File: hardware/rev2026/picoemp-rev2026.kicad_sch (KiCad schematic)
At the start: 53 parts, among them J1 EDGE-SMA, J2 1x2_Pin_Header, J3 MKDS 1,5/2-5.08, J4 EDGE-SMA, P1 Header 7, P2 Header 2, P3 Header 4, Q1 LDA111STR, Q2 RGT16BM65DTL, Q3 AO3422, Q4 AO3422, SW1 KSC741J LFS, SW2 KSC741J LFS, SW3 TL3301AF160QJ, T1 ATB322524, T2 ATB322524, U1 SC0915, U2 74LVC1G17

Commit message: Netclass widths, verified DRC rules, and outline repair
Board setup for routing:

* HV netclass gets real copper -- 0.5 mm default track, 0.8/0.4 via. Its
  clearance stays 0.2 mm; the 1 mm isolation barrier remains a scoped custom
  rule, not a netclass value.
* New Power class (GND, +3V3) at 0.4 mm / 0.8-0.4 via.
* Predefined track widths 0.2/0.3/0.4/0.5/0.8/1.0 and via sizes so W and V
  cycle useful values while routing.

Deliberately NOT splitting an HV_PULSE class out of HV. KiCad 10 resolves each
net to exactly one effective netclass -- an experiment with an overlapping
HV_PULSE showed hasNetclass('HV_PULSE') never matching while hasNetclass('HV')
still did. Splitting the discharge-loop nets out would risk dropping the two
highest-energy nets on the board out of the isolation-barrier rule, to buy
nothing but a router default width. Route those wide by hand or with a pour.

Custom rules, each confirmed to actually fire against this board:

* Barrier and edge rules now use hasNetclass('HV') so they cannot develop a
  hole if a net ever picks up an additional class.
* Advisory (warning-severity) 0.4 mm minimum on HV track width. Advisory
  because KiCad has no auto-neck and necking into a pad is legitimate.
* Documented exceptions for geometry the layout does not control: edge-mount
  SMA pads on J1/J4, ATB3225 intra-package spacing on T1/T2, TO-252 tab-to-lead
  spacing on Q2.

Two DRU behaviours worth recording, both verified rather than assumed:

* The LAST matching rule wins, so exceptions must sit below the broad rules.
  Placed above, they are silently overridden.
* An unknown function in a condition is NOT an error. memberOf() -- the pre-v7
  spelling of memberOfFootprint() -- parses, reports nothing and never matches,
  so a rule can look present while enforcing nothing.

Also repaired the two remaining 0.020 mm Edge.Cuts gaps at the top corners. The
earlier outline fix removed four degenerate stub segments but only re-joined the
two at the bottom, so in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
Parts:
- MH1, MH2, MH3: footprint MountingHole:MountingHole_3.2mm_M3 -> MountingHole:MountingHole_3.2mm_M3_Pad_Via
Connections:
- no-connect marks 27 -> 24

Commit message: Name every net; scope the HV class by an HV_* wildcard
Replaced all 20 auto-generated net names with meaningful ones by adding local
labels to the schematic, and propagated them to the board.

    HV_RAIL       <- Net-(D2-K)        +250 V rail: C3+, D2 K, J1 shell, R2
    HV_RTN        <- Net-(D7-A)        isolated HV return
    HV_RECT       <- Net-(D2-A)        T1 secondary -> D2 anode
    HV_OUT        <- Net-(J1-Ext)      Q2 collector -> SMA centre (the pulse)
    HV_SENSE      <- Net-(J3-Pin_2)    divider tap, J3 pin 2
    HV_SENSE_LED  <- Net-(Q1-A)        R1 -> Q1 opto LED anode
    HV_GATE       <- Net-(D7-K)        Q2 gate, clamped by D7
    HV_GATE_DRV   <- Net-(R7-Pad2)     T2 secondary -> gate series R7
    T1_PRI_A/B, T2_PRI_A/B, PRI_CLAMP, Q3_GATE, Q4_GATE,
    VEXT_IN, VBUS, LED_HV_DET_A, LED_STATUS_A, LED_CHARGE_A

The HV_ prefix is load-bearing, not cosmetic. Every net in the isolated HV
domain now carries it, so a single "HV_*" netclass pattern covers all of them
and a newly added HV net cannot be silently left out of the 1 mm barrier.

That had already happened. The opto LED anode -- then Net-(Q1-A) -- sits
entirely on the HV side of Q1, between R1 and the LED, and was NOT in the HV
class. DRC would have permitted logic copper 0.2 mm from a node that floats
with the HV return. The netlist shows the domain is galvanically isolated: T1,
T2 and Q1 are the only crossings, and GND appears on no HV net.

Verified rather than assumed:
* Net membership is byte-identical for all 20 renamed nets, and the whole
  schematic net partition is unchanged, so connectivity did not move.
* The HV_* wildcard really resolves -- board pads now report netclass 'HV' for
  the renamed nets. A pattern that silently matched nothing would have left the
  barrier inert with no error.
* The symbol->schematic pin transform was not guessed. Scoring pins against
  wire endpoints could not decide it (a symmetric 2-pin part lands on a valid
  endpoint under either convention), so i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
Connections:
- net LED_STATUS_A: now reaches D8.2 (A), R12.2
- net LED_CHARGE_A: now reaches D9.2 (A), R13.2
- net T2_PRI_B: now reaches C5.2, R3.1, T2.4
- net HV_RTN: now reaches C3.1, D7.2 (A), J3.1 (Pin_1), Q1.2 (K), Q2.3 (E), R9.1, SW3.1, T1.3, T2.2
- net HV_SENSE: now reaches J3.2 (Pin_2), R1.1, R2.2, SW3.2
- net PRI_CLAMP: now reaches D3.1 (K), R3.2, R4.2
- net Q3_GATE: now reaches D4.1 (K), Q3.1 (G), R5.2
- net Q4_GATE: now reaches D5.1 (K), Q4.1 (G), R10.2
- net T1_PRI_B: now reaches C1.2, C2.2, R4.1, T1.4
- net HV_RAIL: now reaches C3.2, D2.1 (K), J1.1 (In), R2.1
- net HV_RECT: now reaches D2.2 (A), T1.2
- net HV_GATE: now reaches D7.1 (K), Q2.1 (G), R7.1
- net HV_OUT: now reaches J1.2 (Ext), Q2.2 (C)
- net T1_PRI_A: now reaches Q3.3 (D), T1.1
- net HV_GATE_DRV: now reaches R7.2, R9.2, T2.3
- net LED_HV_DET_A: now reaches D6.2 (A), R11.2
- net T2_PRI_A: now reaches Q4.3 (D), T2.1
- net HV_SENSE_LED: now reaches Q1.1 (A), R1.2
- net VEXT_IN: now reaches D1.2 (A), J2.1 (Pin_1)
- net VBUS: now reaches D1.1 (K), U1.40 (VBUS)
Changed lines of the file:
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@@
 	)
 	(embedded_fonts no)
+	(label "T1_PRI_B"
+		(at 274.32 294.64 0)
+		(effects
+			(font
+				(size 1.27 1.27)
+			)
+			(justify left bottom)
+		)
+	)
+	(label "T2_PRI_B"
+		(at 279.4 353.06 0)
+		(effects
+			(font
+				(size 1.27 1.27)
+			)
+			(justify left bottom)
+		)
+	)
+	(label "VEXT_IN"
+		(at 142.24 52.07 0)
+		(effects
+			(font
+				(size 1.27 1.27)
+			)
+			(justify left bottom)
+		)
+	)
+	(label "VBUS"
+		(at 142.24 57.15 0)
+		(effects
+			(font
+				(size 1.27 1.27)
+			)
+			(justify left bottom)
+		)
+	)
+	(label "HV_RECT"
+		(at 325.12 276.86 0)
+		(effects
+			(font
+				(size 1.27 1.27)
+			)
+			(justify left bottom)
+		)
+	)
+	(label "HV_RAIL"
+		(at 345.44 281.94 0)
+		(effects
+			(font
+				(size 1.27 1.27)
+			)
+			(justify left bottom)
+		)
+	)
+	(label "PRI_CLAMP"
+		(at 193.04 309.88 0)
+		(effects
+			(font
+				(size 1.27 1.27)
+			)
+			(justify left bottom)
+		)
+	)
+	(label "Q3_GATE"
+		(at 233.68 294.64 0)
+		(effects
+			(font
+				(size 1.27 1.27)
+			)
+			(justify left bottom)
+		)
+	)
+	(label "Q4_GATE"
+		(at 228.6 355.6 0)
+		(effects
+			(font
+				(size 1.27 1.27)
+			)
+			(justify left bottom)
+		)
+	)
+	(label "LED_HV_DET_A"
+		(at 69.85 116.84 0)
+		(effects
+			(font
+				(size 1.27 1.27)
+			)
+			(justify left bottom)
+		)
+	)
+	(label "HV_RTN"
+		(at 345.44 287.02 0)
+		(effects
+			(font
+				(size 1.27 1.27)
+			)
+			(justify left bottom)
+		)
+	)
+	(label "HV_GATE"
+		(at 365.76 337.82 0)
+		(effects
+			(font
+				(size 1.27 1.27)
+			)
+			(justify left bottom)
+		)
+	)
+	(label "LED_STATUS_A"
+		(at 69.85 132.08 0)
+		(effects
+			(font
+				(size 1.27 1.27)
+			)
+			(justify left bottom)
+		)
+	)
+	(label "LED_CHARGE_A"
+		(at 229.87 114.3 0)
+		(effects
+			(font
+				(size 1.27 1.27)
+			)
+			(justify left bottom)
+		)
+	)
+	(label "HV_OUT"
+		(at 424.18 276.86 0)
+		(effects
+			(font
+				(size 1.27 1.27)
+			)
+			(justify left bottom)
+		)
+	)
+	(label "HV_SENSE"
+		(at 381 218.44 0)
+		(effects
+			(font
+				(size 1.27 1.27)
+			)
+			(justify left bottom)
+		)
+	)
+	(label "HV_SENSE_LED"
+		(at 317.5 236.22 0)
+		(effects
+			(font
+				(size 1.27 1.27)
+			)
+			(justify left bottom)
+		)
+	)
+	(label "T1_PRI_A"
+		(at 261.62 287.02 0)
+		(effects
+			(font
+				(size 1.27 1.27)
+			)
+			(justify left bottom)
+		)
+	)
+	(label "T2_PRI_A"
+		(at 261.62 350.52 0)
+		(effects
+			(font
+				(size 1.27 1.27)
+			)
+			(justify left bottom)
+		)
+	)
+	(label "HV_GATE_DRV"
+		(at 347.98 335.28 0)
+		(effects
+			(font
+				(size 1.27 1.27)
+			)
+			(justify left bottom)
+		)
+	)
 )

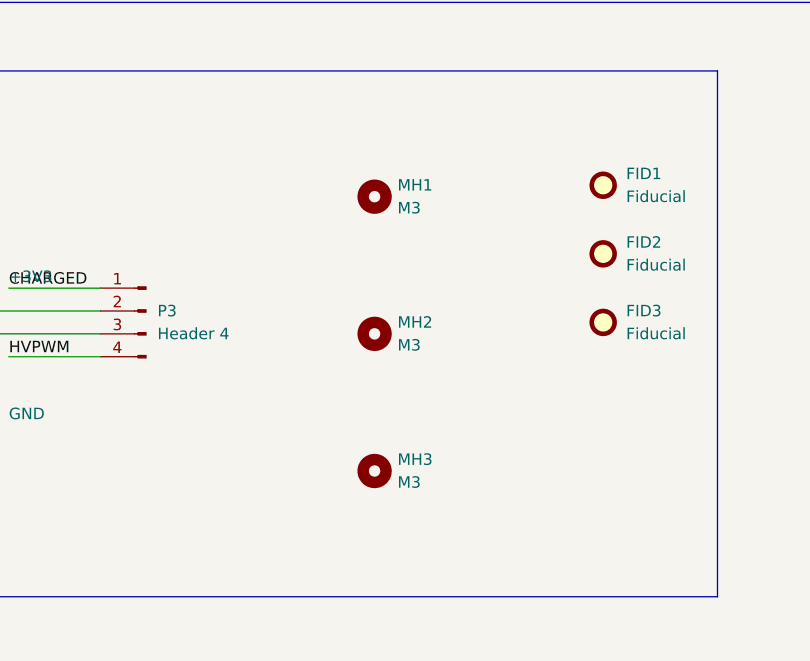
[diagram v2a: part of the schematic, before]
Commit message: Move isolation slots outboard; fix inert HV netclass; restore pinless MH1-3
Board geometry:
* Both isolation slots moved 3.000 mm outboard and shortened to end at
  y=135.200, clear of the M3 holes. Island width 21.184 -> 27.184 mm, with a
  5.32 mm west strip and 4.96 mm east strip remaining.
* The left slot was a parallelogram -- its outer wall ran from x=112.711 at the
  bottom to x=112.737 at the top, a 0.026 mm skew over 36.7 mm inherited from
  the Altium import. Rebuilt as a true rectangle.
* The staggered notches above each slot moved with them and had their Y squared
  up; left sat at 96.3536/99.3 and right at 96.3728/99.3192, 0.019 mm of pure
  import noise.
* East edge was two collinear segments split at y=141.872; merged into one.
* MH1/MH2 were 0.095 mm off centre (3.905 / 4.095 mm from the side edges).
  Shifting BOTH by +0.095 keeps their 32.000 mm spacing -- which is the Hammond
  1551B shield boss spacing, inherited from upstream's hi-pot-validated layout
  and NOT free to change -- and lands them at exactly 4.000 mm from each edge.
  MH3 has no such constraint and moved to a matching 4.000 mm corner inset.

This clears the J3 copper-into-slot violation without touching J3.

THE HV NETCLASS WAS ENFORCING NOTHING. The nets were renamed in the .kicad_pcb
directly as bare 'HV_RAIL', with a wildcard 'HV_*' pattern written to match.
Update PCB from Schematic then rewrote them to KiCad's canonical root-sheet form
'/HV_RAIL', and the pattern stopped matching anything at all. The class covered
zero nets, the 1 mm isolation barrier enforced nothing, and nothing anywhere
reported an error -- DRC simply listed the offending HV pads as netclass
'Default'. Patterns are now explicit '/HV_*' names, and a new test checks them
against the net names actually present in the .kicad_pcb rather than against a
hardcoded list, because a hardcoded list drifts along with the pattern it is
supposed to be checking.

Explicit rather than a '/HV_*' wildcard, because that wildcar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
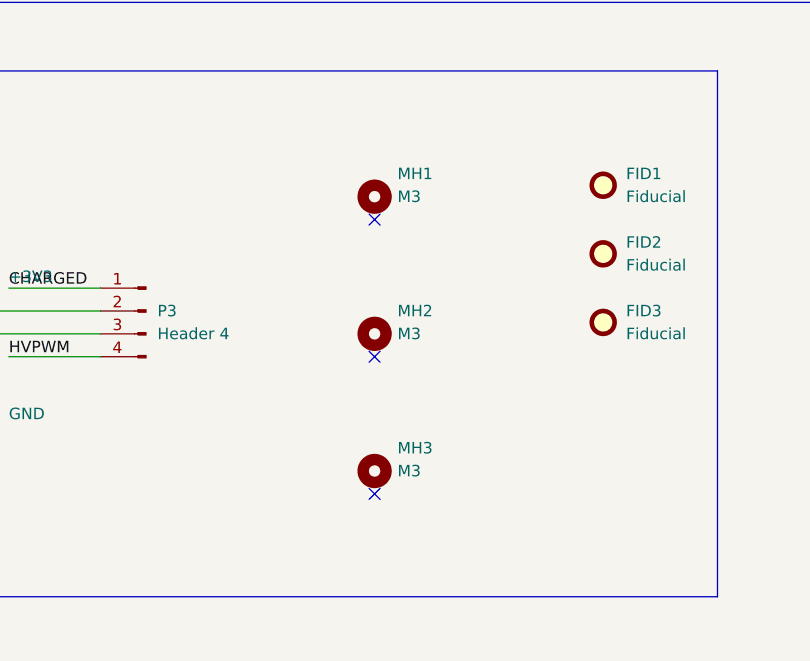
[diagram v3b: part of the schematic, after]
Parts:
- MH1, MH2, MH3: footprint MountingHole:MountingHole_3.2mm_M3_Pad_Via -> MountingHole:MountingHole_3.2mm_M3
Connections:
- no-connect marks 24 -> 27

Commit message: Checkpoint before HV placement redistribution
Snapshot taken at the user's request so the placement work that follows is easy
to revert in one step.

Co-Authored-By: Claude Opus 5 <noreply@anthropic.com>
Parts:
- MH1, MH2, MH3: footprint MountingHole:MountingHole_3.2mm_M3 -> MountingHole:MountingHole_3.2mm_M3_Pad_Via; symbol Mechanical:MountingHole -> Mechanical:MountingHole_Pad
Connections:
- net GND: now also MH3.1
- no-connect marks 27 -> 26
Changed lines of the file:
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@@
 	)
 	(no_connect
-		(at 123.19 228.6)
-	)
-	(no_connect
 		(at 165.1 88.9)
 	)
@@
 	)
 	(no_connect
+		(at 123.19 198.12)
+	)
+	(no_connect
 		(at 119.38 139.7)
 	)
@@
 	)
 	(no_connect
-		(at 123.19 198.12)
-	)
-	(no_connect
 		(at 165.1 99.06)
 	)
@@
 	(symbol
 		(lib_id "power:GND")
+		(at 80.01 218.44 0)
+		(unit 1)
+		(body_style 1)
+		(exclude_from_sim no)
+		(in_bom yes)
+		(on_board yes)
+		(in_pos_files yes)
+		(dnp no)
+		(fields_autoplaced yes)
+		(property "Reference" "#PWR013"
+			(at 80.01 224.79 0)
+			(hide yes)
+			(show_name no)
+			(do_not_autoplace no)
+			(effects
+				(font
+					(size 1.27 1.27)
+				)
+			)
+		)
+		(property "Value" "GND"
+			(at 80.01 223.52 0)
+			(show_name no)
+			(do_not_autoplace no)
+			(effects
+				(font
+					(size 1.27 1.27)
+				)
+			)
+		)
+		(property "Footprint" ""
+			(at 80.01 218.44 0)
+			(hide yes)
+			(show_name no)
+			(do_not_autoplace no)
+			(effects
+				(font
+					(size 1.27 1.27)
+				)
+			)
+		)
+		(property "Datasheet" ""
+			(at 80.01 218.44 0)
+			(hide yes)
+			(show_name no)
+			(do_not_autoplace no)
+			(effects
+				(font
+					(size 1.27 1.27)
+				)
+			)
+		)
+		(property "Description" "Power symbol creates a global label with name \"GND\" , ground"
+			(at 80.01 218.44 0)
+			(hide yes)
+			(show_name no)
+			(do_not_autoplace no)
+			(effects
+				(font
+					(size 1.27 1.27)
+				)
+			)
+		)
+		(pin "1"
+		)
+		(instances
+			(project "picoemp-rev2026"
+				(path "/2587a454-e9b8-4dd2-940e-91a5ec62d2c9"
+					(reference "#PWR013")
+					(unit 1)
+				)
+			)
+		)
+	)
+	(symbol
+		(lib_id "power:GND")
 		(at 165.1 139.7 0)
 		(unit 1)
@@
 	)
 	(symbol
-		(lib_id "Mechanical:MountingHole")
+		(lib_id "Mechanical:MountingHole_Pad")
 		(at 123.19 210.82 0)
 		(unit 1)
@@
 			)
 		)
-		(property "Footprint" "MountingHole:MountingHole_3.2mm_M3"
+		(property "Footprint" "MountingHole:MountingHole_3.2mm_M3_Pad_Via"
 			(at 123.19 210.82 0)
 			(hide yes)
@@
 			)
 		)
+		(pin "1"
+		)
 		(instances
 			(project "picoemp-rev2026"
@@
 	)
 	(symbol
-		(lib_id "power:GND")
-		(at 80.01 218.44 0)
-		(unit 1)
-		(body_style 1)
-		(exclude_from_sim no)
-		(in_bom yes)
-		(on_board yes)
-		(in_pos_files yes)
-		(dnp no)
-		(fields_autoplaced yes)
-		(property "Reference" "#PWR013"
-			(at 80.01 218.44 0)
-			(hide yes)
-			(show_name no)
-			(do_not_autoplace no)
-			(effects
-				(font
-					(size 1.27 1.27)
-				)
-			)
-		)
-		(property "Value" "GND"
-			(at 82.55 219.7099 0)
-			(show_name no)
-			(do_not_autoplace no)
-			(effects
-				(font
-					(size 1.27 1.27)
-				)
-				(justify left)
-			)
-		)
-		(property "Footprint" ""
-			(at 80.01 218.44 0)
-			(hide yes)
-			(show_name no)
-			(do_not_autoplace no)
-			(effects
-				(font
-					(size 1.27 1.27)
-				)
-			)
-		)
-		(property "Datasheet" ""
-			(at 80.01 218.44 0)
-			(hide yes)
-			(show_name no)
-			(do_not_autoplace no)
-			(effects
-				(font
-					(size 1.27 1.27)
-				)
-			)
-		)
-		(property "Description" "Power symbol creates a global label with name \"GND\" , ground"
-			(at 80.01 218.44 0)
-			(hide yes)
-			(show_name no)
-			(do_not_autoplace no)
-			(effects
-				(font
-					(size 1.27 1.27)
-				)
-			)
-		)
-		(pin "1"
-		)
-		(instances
-			(project "picoemp-rev2026"
-				(path "/2587a454-e9b8-4dd2-940e-91a5ec62d2c9"
-					(reference "#PWR013")
-					(unit 1)
-				)
-			)
-		)
-	)
-	(symbol
 		(lib_id "Device:R_Small")
 		(at 337.82 77.47 0)
@@
 	)
 	(symbol
-		(lib_id "Mechanical:MountingHole")
+		(lib_id "Mechanical:MountingHole_Pad")
 		(at 123.19 195.58 0)
 		(unit 1)
@@
 			)
 		)
-		(property "Footprint" "MountingHole:MountingHole_3.2mm_M3"
+		(property "Footprint" "MountingHole:MountingHole_3.2mm_M3_Pad_Via"
 			(at 123.19 195.58 0)
 			(hide yes)
@@
 			)
 		)
+		(pin "1"
+		)
 		(instances
 			(project "picoemp-rev2026"
@@
 	)
 	(symbol
+		(lib_id "power:GND")
+		(at 123.19 228.6 0)
+		(unit 1)
+		(body_style 1)
+		(exclude_from_sim no)
+		(in_bom yes)
+		(on_board yes)
+		(in_pos_files yes)
+		(dnp no)
+		(fields_autoplaced yes)
+		(property "Reference" "#PWR018"
+			(at 123.19 234.95 0)
+			(hide yes)
+			(show_name no)
+			(do_not_autoplace no)
+			(effects
+				(font
+					(size 1.27 1.27)
+				)
+			)
+		)
+		(property "Value" "GND"
+			(at 123.19 233.68 0)
+			(show_name no)
+			(do_not_autoplace no)
+			(effects
+				(font
+					(size 1.27 1.27)
+				)
+			)
+		)
+		(property "Footprint" ""
+			(at 123.19 228.6 0)
+			(hide yes)
+			(show_name no)
+			(do_not_autoplace no)
+			(effects
+				(font
+					(size 1.27 1.27)
+				)
+			)
+		)
+		(property "Datasheet" ""
+			(at 123.19 228.6 0)
+			(hide yes)
+			(show_name no)
+			(do_not_autoplace no)
+			(effects
+				(font
+					(size 1.27 1.27)
+				)
+			)
+		)
+		(property "Description" "Power symbol creates a global label with name \"GND\" , ground"
+			(at 123.19 228.6 0)
+			(hide yes)
+			(show_name no)
+			(do_not_autoplace no)
+			(effects
+				(font
+					(size 1.27 1.27)
+				)
+			)
+		)
+		(pin "1"
+		)
+		(instances
+			(project "picoemp-rev2026"
+				(path "/2587a454-e9b8-4dd2-940e-91a5ec62d2c9"
+					(reference "#PWR018")
+					(unit 1)
+				)
+			)
+		)
+	)
+	(symbol
 		(lib_id "Connector:Conn_Coaxial_Power")
 		(at 419.1 276.86 90)
@@
 		(in_pos_files yes)
 		(dnp no)
-		(fields_autoplaced yes)
 		(property "Reference" "#PWR012"
 			(at 80.01 205.74 0)
@@
 		)
 		(property "Value" "+3V3"
-			(at 82.55 204.4699 0)
+			(at 77.47 201.422 0)
 			(show_name no)
 			(do_not_autoplace no)
@@
 	)
 	(symbol
-		(lib_id "Mechanical:MountingHole")
+		(lib_id "Mechanical:MountingHole_Pad")
 		(at 123.19 226.06 0)
 		(unit 1)
@@
 			)
 		)
-		(property "Footprint" "MountingHole:MountingHole_3.2mm_M3"
+		(property "Footprint" "MountingHole:MountingHole_3.2mm_M3_Pad_Via"
 			(at 123.19 226.06 0)
 			(hide yes)
@@
 			)
 		)
+		(pin "1"
+		)
 		(instances

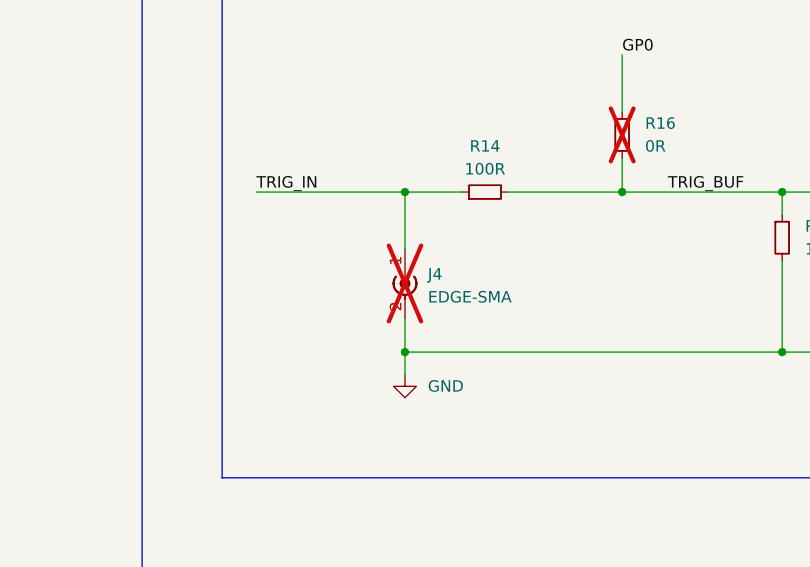
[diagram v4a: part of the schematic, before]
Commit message: Pull the barrier-limited HV tracks back to 1.150 mm
All five ended on a transformer secondary pad, whose centre sits 1.770 mm from
the primary pad centre of the same package. A 0.5 mm track centred there lands
1.020 mm from the primary pad edge -- passing the 1.000 mm barrier in CAD, but
leaving 0.020 mm for etch tolerance. Standard trace-width tolerance is around
+/-20%, which on a 0.5 mm track is +/-0.05 mm per edge, so the barrier could be
violated in production while passing in the file.

Moved those endpoints 0.130 mm further from the primary row. They stay well
inside the secondary pad (0.370 mm from its far edge), so connectivity is
untouched -- verified beforehand that exactly five segments and no vias reach
those four points.

One needed 0.145 mm rather than 0.130: /HV_RTN leaving T1.3 runs west while T1.4
sits directly above its start, so moving only one end left the segment sloped and
its closest approach, at the pad's west edge, came out at 1.141 mm.

Tightest HV-to-foreign clearance is now 1.150 mm at the transformers, up from
1.020. DRC still 0 errors, 0 warnings, 0 unconnected, parity clean.

Not touched: /HV_GATE runs 1.060 mm from MH1's pad in two places. That was not
in the five, it has three times the margin, and the track is a long vertical
with shared endpoints so pulling it cascades. Worth noting MH1's pad is floating
copper -- unconnected -- sitting beside a 250 V node.

Co-Authored-By: Claude Opus 5 <noreply@anthropic.com>
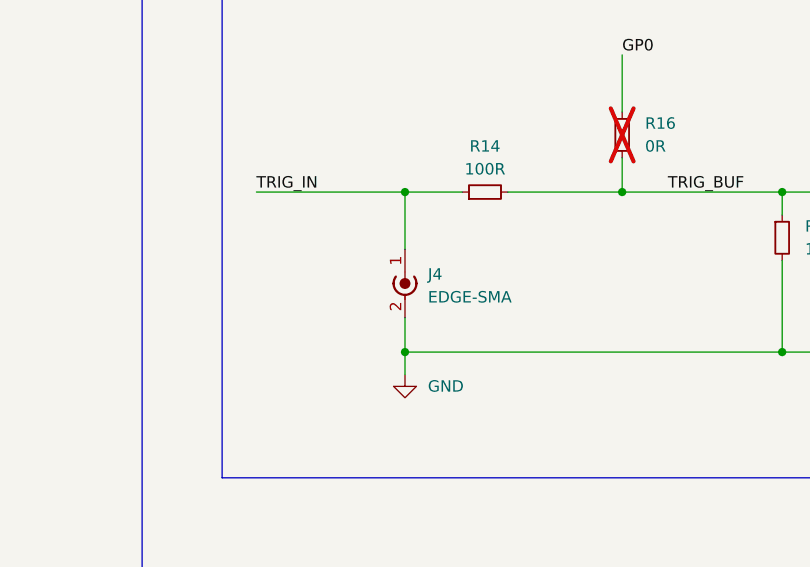
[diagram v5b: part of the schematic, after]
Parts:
- J4: now fitted
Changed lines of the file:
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@@
 		(on_board yes)
 		(in_pos_files yes)
-		(dnp yes)
+		(dnp no)
 		(fields_autoplaced yes)
 		(property "Reference" "J4"
